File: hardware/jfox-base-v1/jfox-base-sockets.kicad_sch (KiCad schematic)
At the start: 3 parts, among them J1 Mezz A, J2 Mezz B, J3 Mezz C

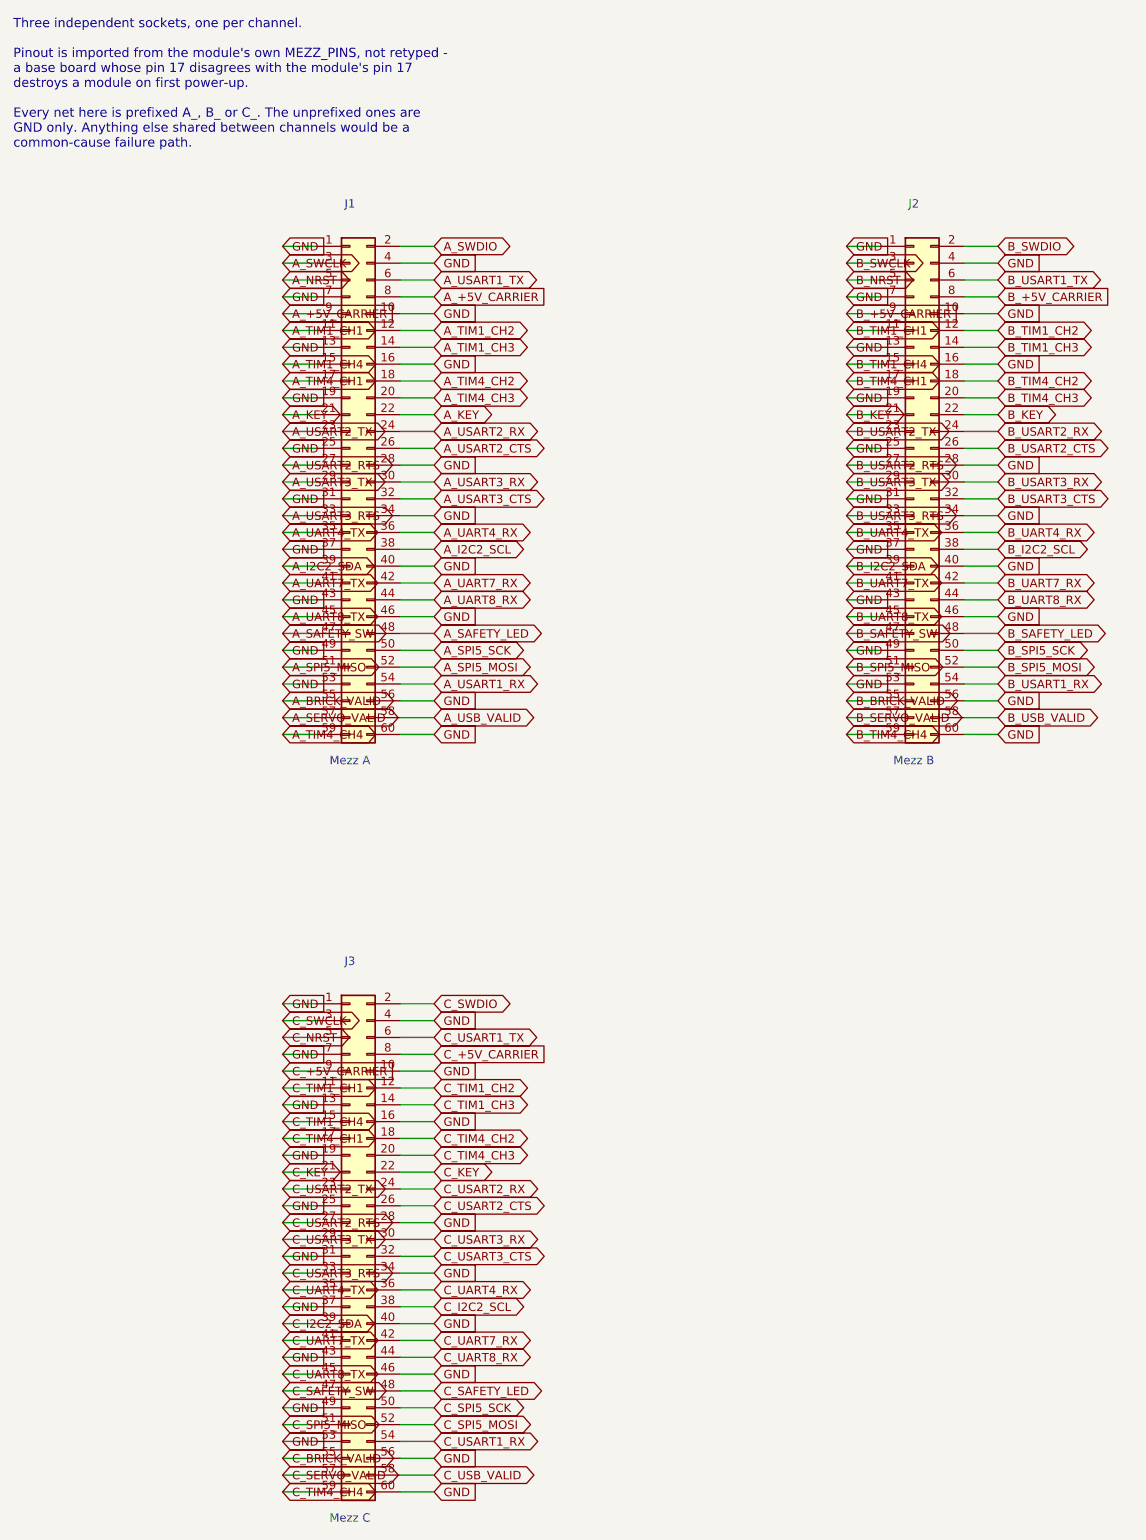
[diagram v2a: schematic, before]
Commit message: Provability: check the backplane, and fix the four defects that found
Nothing read JFOX-BASE-v1. Every checker in hardware/tools/ opened
jfox-fmu-v1/jfox-fmu.kicad_sch and only that, so no claim about the
backplane was provable - including the ones the requirements table recorded
as verified.

check_base_schematic.py now reads it: fused rails must reach a card socket,
the LTC4417 divider must produce the window it claims, that window must fit
every part downstream, and the feed-health outputs must reach a card AND be
driven. It failed on first run, which is the only reason to trust it.

What it found, in the order it found them:

  1. THE CARDS HAD NO POWER. The fuses put out A/B/C_FUSED and the card edge
     reads +5V_CARRIER. Both boards generated cleanly, both passed DRC, and
     the two halves were never connected to each other. The chain now
     terminates on the card rail past the shunt, not before it.

  2. THE FEEDS ARE NOT BATTERIES. VBAT_RH/VBAT_LH carry 5 V - the thresholds
     said so and the connectors are labelled PWR. Renamed PWR1_IN/PWR2_IN,
     output PWR_ORED. The name was the thing that was wrong.

  3. THE WINDOW PASSED MORE THAN A PART SURVIVES, and the binding part was
     not the one found by hand. The analysis flagged the AP2112K at 6.0 V
     against a 5.81 V threshold - 190 mV. The checker compared against every
     downstream part and found the ISOW1044 at 5.5 V: NEGATIVE 310 mV. A
     feed the controller reported as good would have destroyed the isolator.

     787k / 28k7 / 196k -> UV 4.50 V, OV 5.16 V
       ISOW1044  +338 mV      AP2112K  +838 mV

  4. THE ORING CONTROLLER'S OUTPUT WAS NEVER CONNECTED. Its pin map was
     written from the datasheet's block diagram, not the symbol: the pins
     are ~{VALID1..3} with overbars, VOUT not OUT, HYS not HYST, and there
     is no STAT pin at all. nets.get() returns None for an unknown key, so
     six pins were silently left unwired - VOUT among them. PWR_ORED was fed
     only by D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
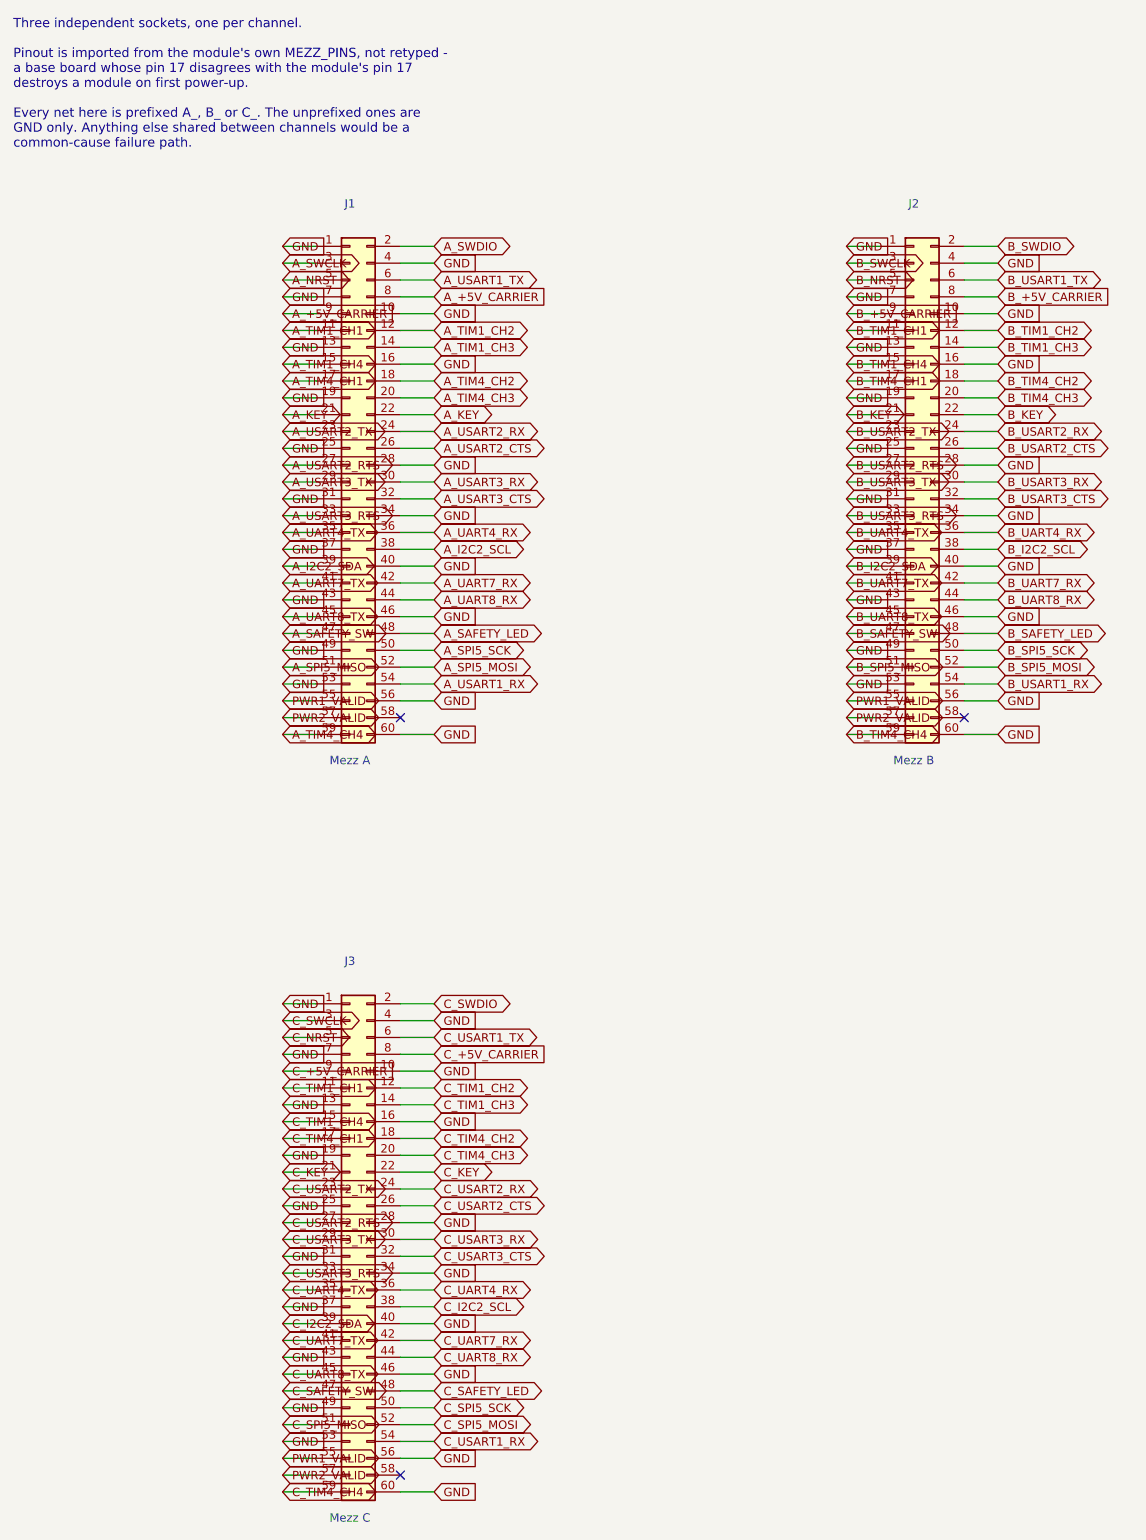
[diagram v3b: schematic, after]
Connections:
- net B_BRICK_VALID is gone; now on net PWR1_VALID: J2.55 (Pin_55)
- net B_SERVO_VALID is gone; now on net PWR2_VALID: J2.57 (Pin_57)
- net C_BRICK_VALID is gone; now on net PWR1_VALID: J3.55 (Pin_55)
- net C_SERVO_VALID is gone; now on net PWR2_VALID: J3.57 (Pin_57)
- net A_BRICK_VALID renamed PWR1_VALID
- net A_SERVO_VALID renamed PWR2_VALID
- net A_USB_VALID: no longer names the net of J1.58 (Pin_58)
- net B_USB_VALID: no longer names the net of J2.58 (Pin_58)
- net C_USB_VALID: no longer names the net of J3.58 (Pin_58)
- no-connect marks 0 -> 3
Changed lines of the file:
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@@
 		(instances
 			(project "jfox-base"
-				(path "/04508df7-0c5e-4eb6-bdf5-f94c06630641"
+				(path "/1576e18e-51cb-4126-9486-cdd02ae88021"
 					(reference "J1")
 					(unit 1)
@@
 		)
 	)
-	(global_label "A_BRICK_VALID"
+	(global_label "PWR1_VALID"
 		(shape bidirectional)
 		(at 62.23 116.84 0)
@@
 		)
 	)
-	(global_label "A_SERVO_VALID"
+	(global_label "PWR2_VALID"
 		(shape bidirectional)
 		(at 62.23 119.38 0)
@@
 		)
 	)
-	(wire
-		(pts
-			(xy 80.01 119.38) (xy 85.09 119.38)
-		)
-		(stroke
-			(width 0)
-			(type default)
-		)
-	)
-	(global_label "A_USB_VALID"
-		(shape bidirectional)
-		(at 85.09 119.38 180)
-		(fields_autoplaced yes)
-		(effects
-			(font
-				(size 1.27 1.27)
-			)
-			(justify left)
-		)
+	(no_connect
+		(at 80.01 119.38)
 	)
 	(wire
@@
 		(instances
 			(project "jfox-base"
-				(path "/04508df7-0c5e-4eb6-bdf5-f94c06630641"
+				(path "/1576e18e-51cb-4126-9486-cdd02ae88021"
 					(reference "J2")
 					(unit 1)
@@
 		)
 	)
-	(global_label "B_BRICK_VALID"
+	(global_label "PWR1_VALID"
 		(shape bidirectional)
 		(at 147.32 116.84 0)
@@
 		)
 	)
-	(global_label "B_SERVO_VALID"
+	(global_label "PWR2_VALID"
 		(shape bidirectional)
 		(at 147.32 119.38 0)
@@
 		)
 	)
-	(wire
-		(pts
-			(xy 165.1 119.38) (xy 170.18 119.38)
-		)
-		(stroke
-			(width 0)
-			(type default)
-		)
-	)
-	(global_label "B_USB_VALID"
-		(shape bidirectional)
-		(at 170.18 119.38 180)
-		(fields_autoplaced yes)
-		(effects
-			(font
-				(size 1.27 1.27)
-			)
-			(justify left)
-		)
+	(no_connect
+		(at 165.1 119.38)
 	)
 	(wire
@@
 		(instances
 			(project "jfox-base"
-				(path "/04508df7-0c5e-4eb6-bdf5-f94c06630641"
+				(path "/1576e18e-51cb-4126-9486-cdd02ae88021"
 					(reference "J3")
 					(unit 1)
@@
 		)
 	)
-	(global_label "C_BRICK_VALID"
+	(global_label "PWR1_VALID"
 		(shape bidirectional)
 		(at 62.23 231.14 0)
@@
 		)
 	)
-	(global_label "C_SERVO_VALID"
+	(global_label "PWR2_VALID"
 		(shape bidirectional)
 		(at 62.23 233.68 0)
@@
 		)
 	)
-	(wire
-		(pts
-			(xy 80.01 233.68) (xy 85.09 233.68)
-		)
-		(stroke
-			(width 0)
-			(type default)
-		)
-	)
-	(global_label "C_USB_VALID"
-		(shape bidirectional)
-		(at 85.09 233.68 180)
-		(fields_autoplaced yes)
-		(effects
-			(font
-				(size 1.27 1.27)
-			)
-			(justify left)
-		)
+	(no_connect
+		(at 80.01 233.68)
 	)
 	(wire
